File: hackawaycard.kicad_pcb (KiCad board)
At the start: 2 copper layers, 60 x 105 mm, 1 part

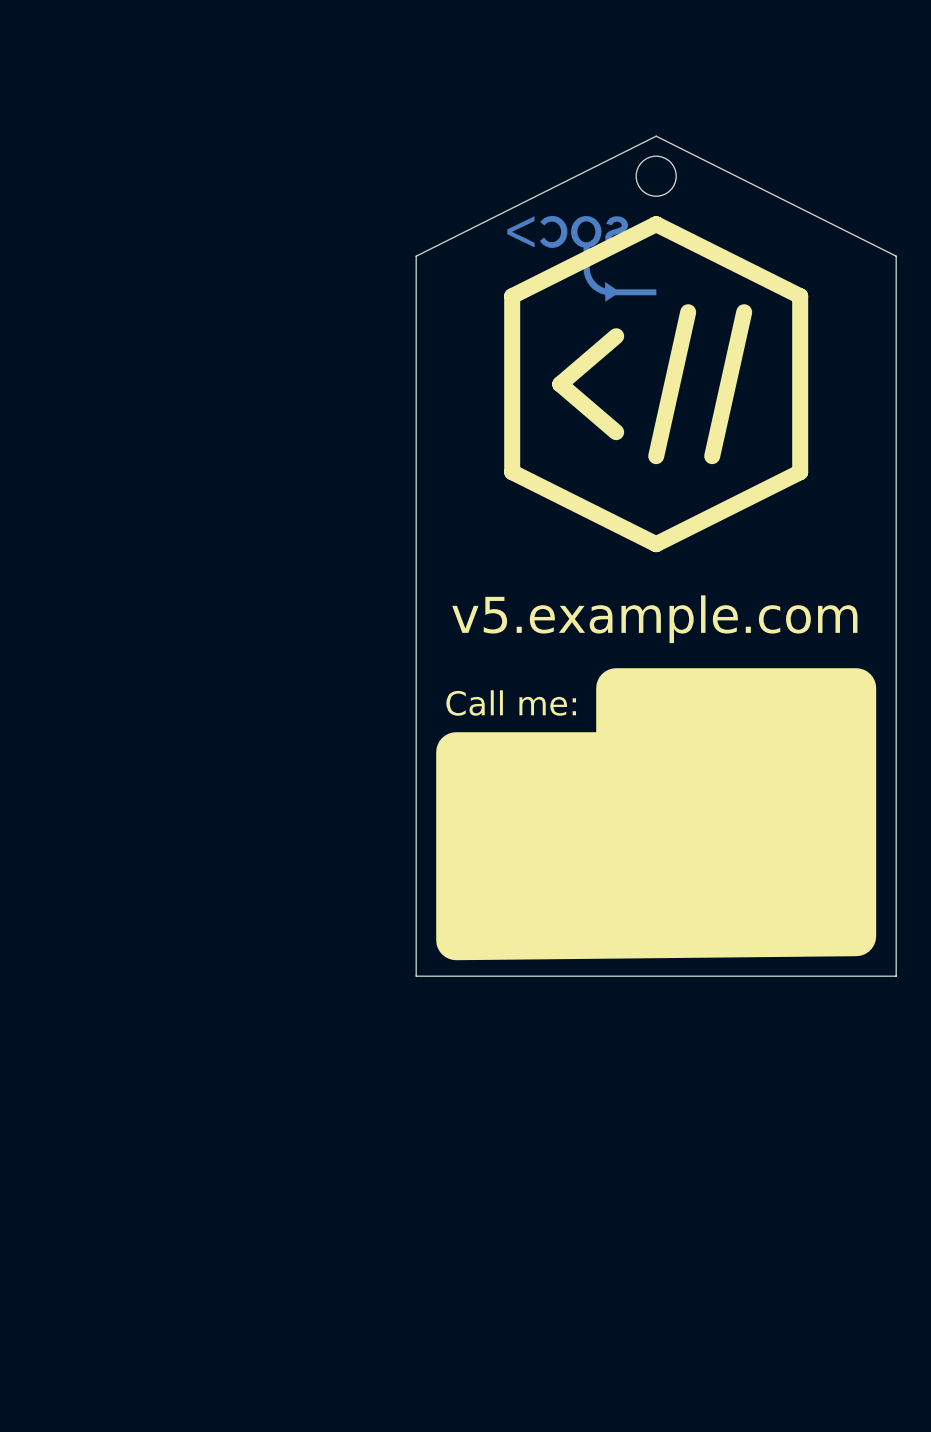
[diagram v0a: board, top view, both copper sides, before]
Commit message: Update hackaway logo to copper, make larger white section
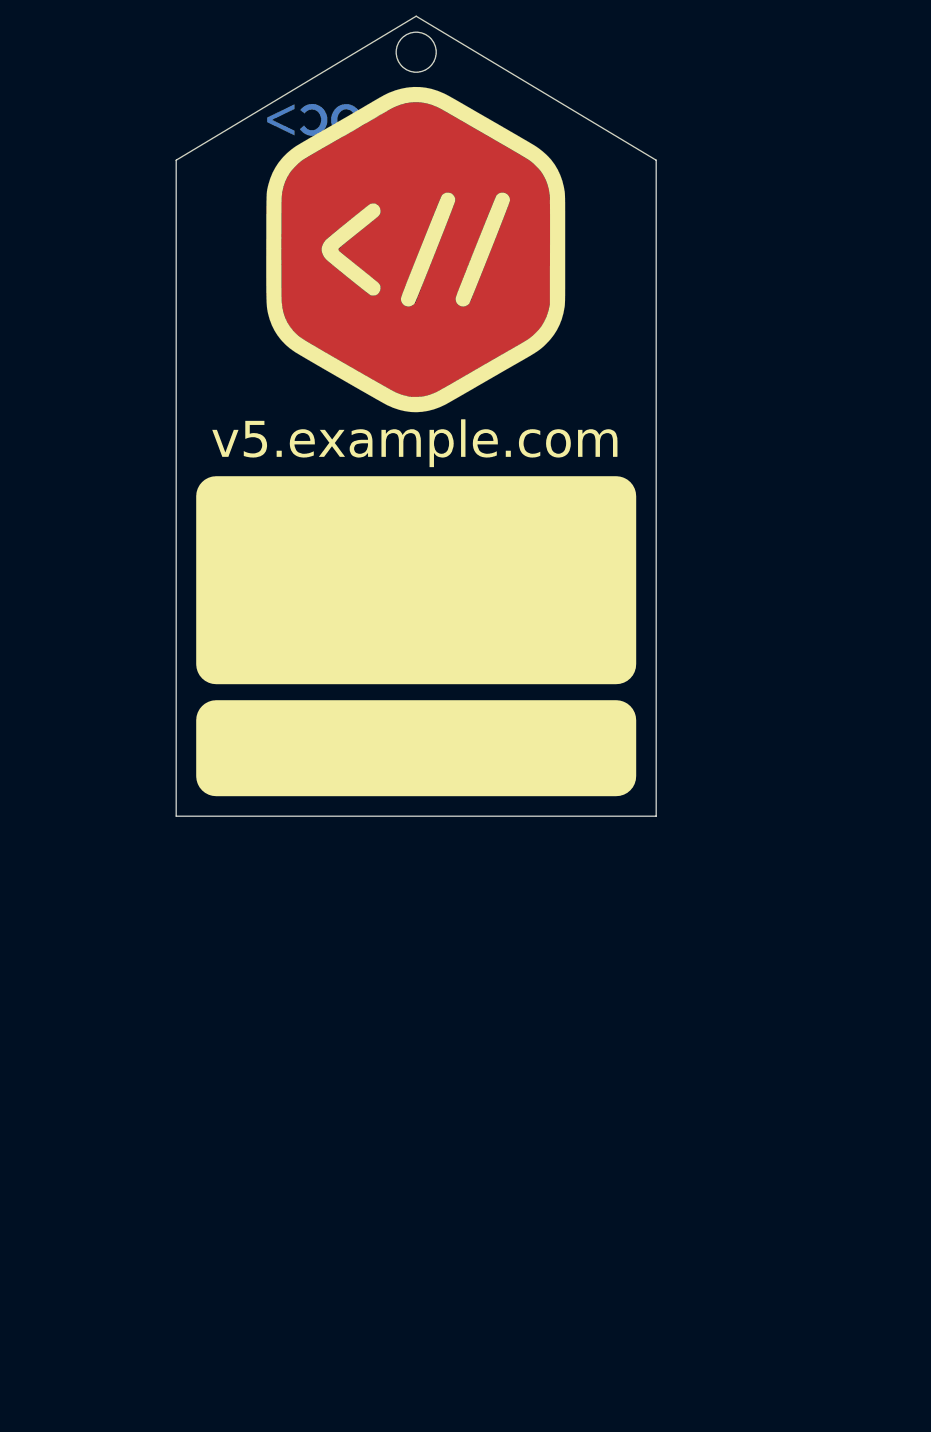
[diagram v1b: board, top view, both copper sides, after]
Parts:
- added G***: LOGO, hackaway:hackaway_copper, F.Cu at (119.5, 89.2)
- moved G*** 33.1 mm to (98.5, 77.0)
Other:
- board size 60 x 105 mm -> 60 x 100 mm
- board text removed: "Call me:"

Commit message: populate the back with stuff
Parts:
- added ?: Pull Request, hackaway:merge_request, F.Cu at (119.0, 74.0)
- added G***: LOGO, hackaway:qr, B.Cu at (80.0, 147.0)
- moved G*** 70.6 mm to (107.5, 147.0)
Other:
- board text added: "2022"
- board text added: "5th - 6th February 2022 Royal Holloway University of London"
- board text added: "Hackaway V5"
- board text added: "example.com/badge_secret?answer=[decimal integer]"
- board text added: "insert sponsors here"

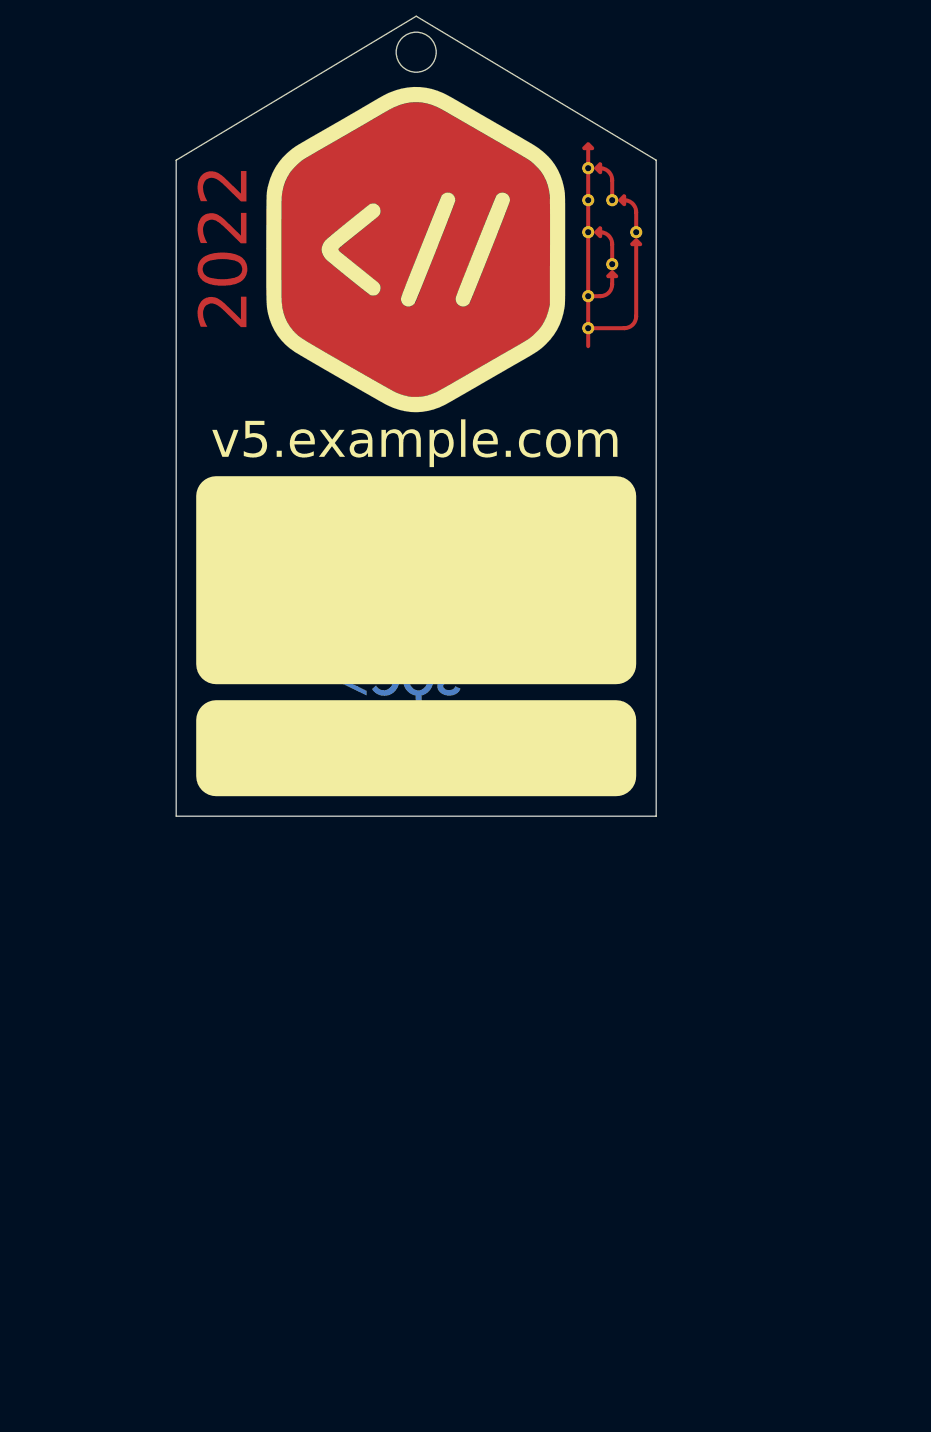
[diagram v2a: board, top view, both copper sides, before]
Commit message: Round off the PCB
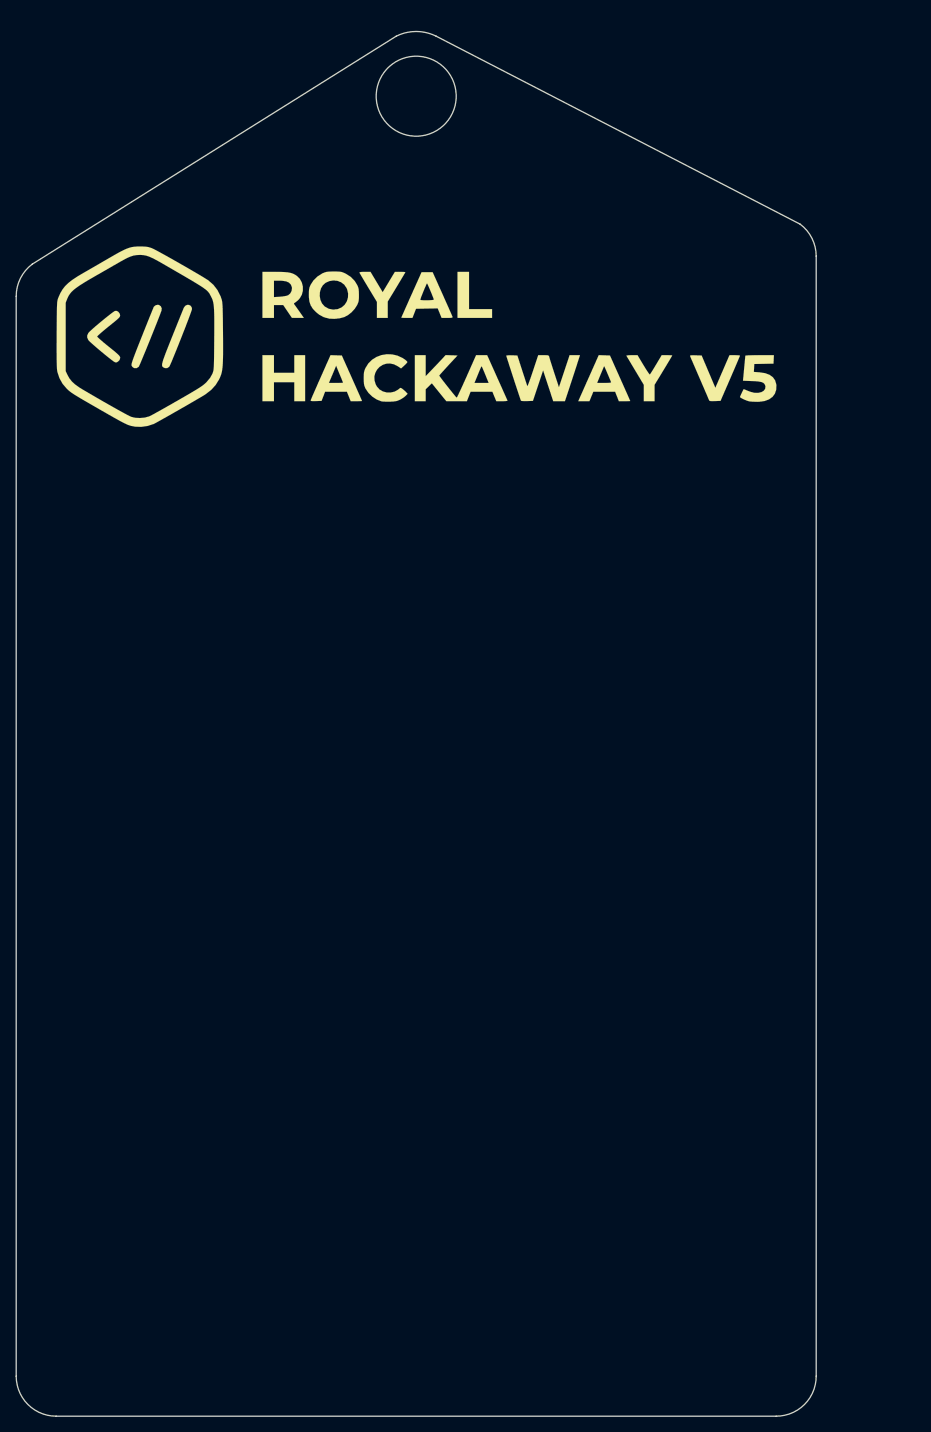
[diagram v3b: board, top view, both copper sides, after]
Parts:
- removed ?: Pull Request, hackaway:merge_request
- removed the G*** at (80.0, 147.0)
- removed the G*** at (119.5, 89.2)
- removed the G*** at (107.5, 147.0)
- added G***: LOGO, hackaway:v5, F.Cu at (100.0, 100.0)
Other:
- board size 60 x 100 mm -> 100 x 173.1 mm
- board text added: "00:00 Midnight Pizza 08:00 Breakfast 10:30 Submissions Open 13:00 Hacking Ends 13:00 Lunch 12:00 Lunchtime 16:00 Presentations/Closing Ceremony"
- board text added: "08:00 Registration Opens 09:30 Opening Ceremony 10:00 Hacking Begins 11:00 Introduction to GitHub 12:00 Lunchtime 18:00 Dinner 20:00 MLH Minigame 22:00 Carrot in a Box"
- board text added: "Sat 5th Feb - Day 1"
- board text added: "Sun 6th Feb - Day 2"
- board text added: "https://wiki.hackaway.dev/"
- board text removed: "2022"
- board text removed: "5th - 6th February 2022 Royal Holloway University of London"
- board text removed: "Hackaway V5"
- board text removed: "example.com/badge_secret?answer=[decimal integer]"
- board text removed: "insert sponsors here"
- board text removed: "v5.example.com"

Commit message: Update Hackaway version number
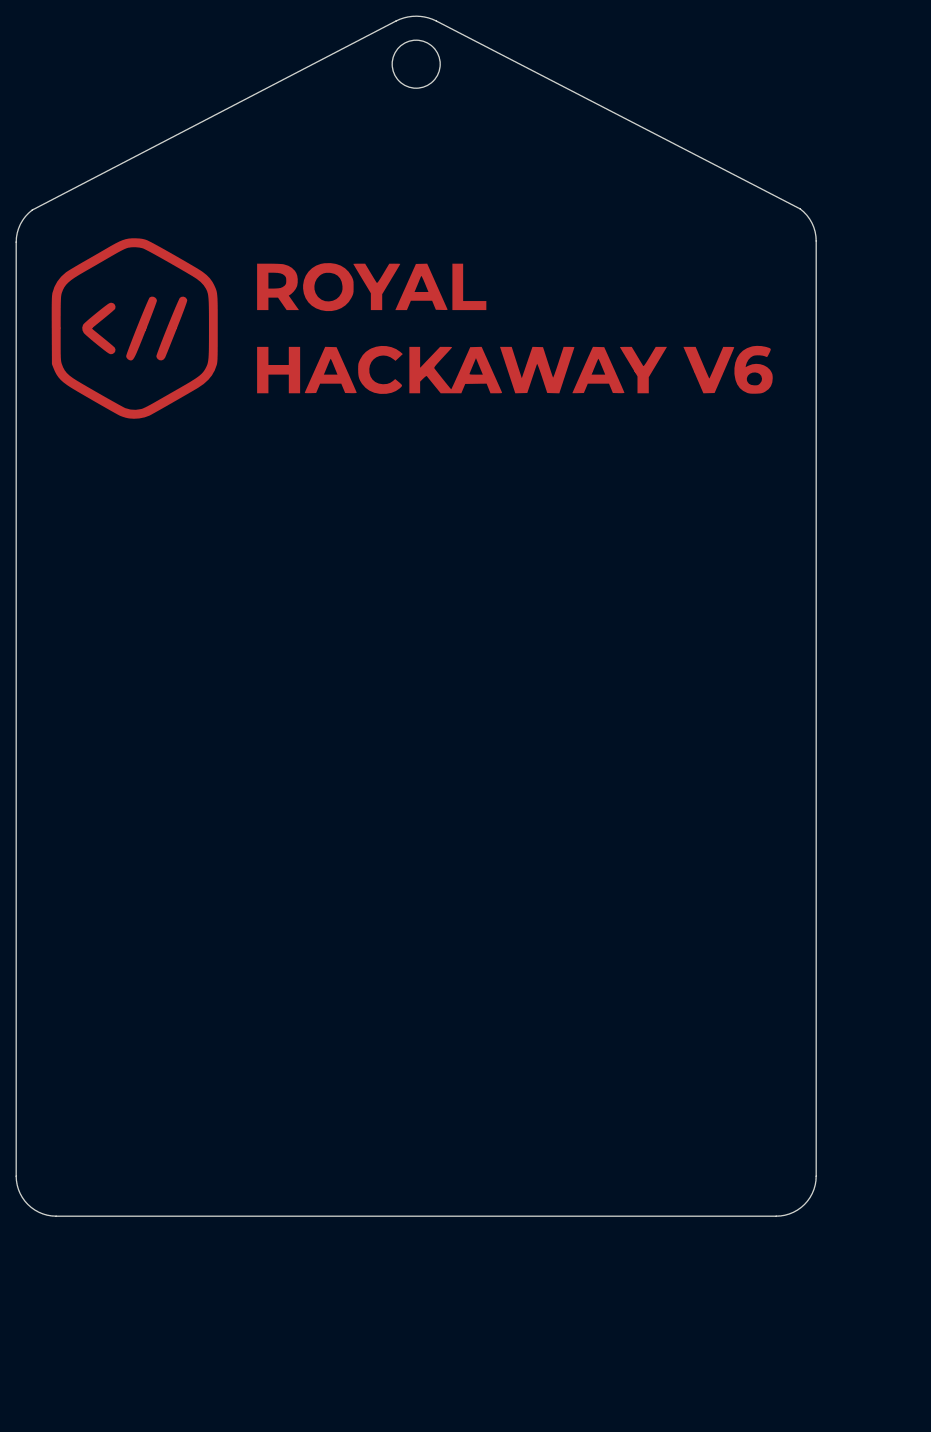
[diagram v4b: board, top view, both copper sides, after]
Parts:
- removed G***: LOGO, hackaway:v5
- added  : , hackaway:havkaway_v6, F.Cu at (99.5, 99.0)
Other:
- board size 100 x 173.1 mm -> 100 x 150 mm
- net class Default removed
- board text added: "00:00 Shout at Tayma 07:00 Call Josh every 2 seconds 12:00 Get Josh out of the lift 13:00 Lunch 16:00 RMT Rail Strike Action Picket"
- board text added: "08:00 Registration Opens 09:30 Opening Ceremony 10:00 Hacking Begins 11:00 Introduction to GitHub 12:00 Lunchtime 18:00 Dinner 19:00 HackathonsUK Minigame 20:00 MLH Minigame 22:00 Carrot in a Box"
- board text added: "Sat 4th Feb - Day 1"
- board text added: "Sun 5th Feb - Day 2"
- board text added: "royalhackaway.com/v6 twitch.tv/hackathonsuk"
- board text removed: "00:00 Midnight Pizza 08:00 Breakfast 10:30 Submissions Open 13:00 Hacking Ends 13:00 Lunch 12:00 Lunchtime 16:00 Presentations/Closing Ceremony"
- board text removed: "08:00 Registration Opens 09:30 Opening Ceremony 10:00 Hacking Begins 11:00 Introduction to GitHub 12:00 Lunchtime 18:00 Dinner 20:00 MLH Minigame 22:00 Carrot in a Box"
- board text removed: "Sat 5th Feb - Day 1"
- board text removed: "Sun 6th Feb - Day 2"
- board text removed: "https://wiki.hackaway.dev/"
